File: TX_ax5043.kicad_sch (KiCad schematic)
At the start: 33 parts, among them P101 U_FL, U156 AX5043, U89 TPS22917DBV

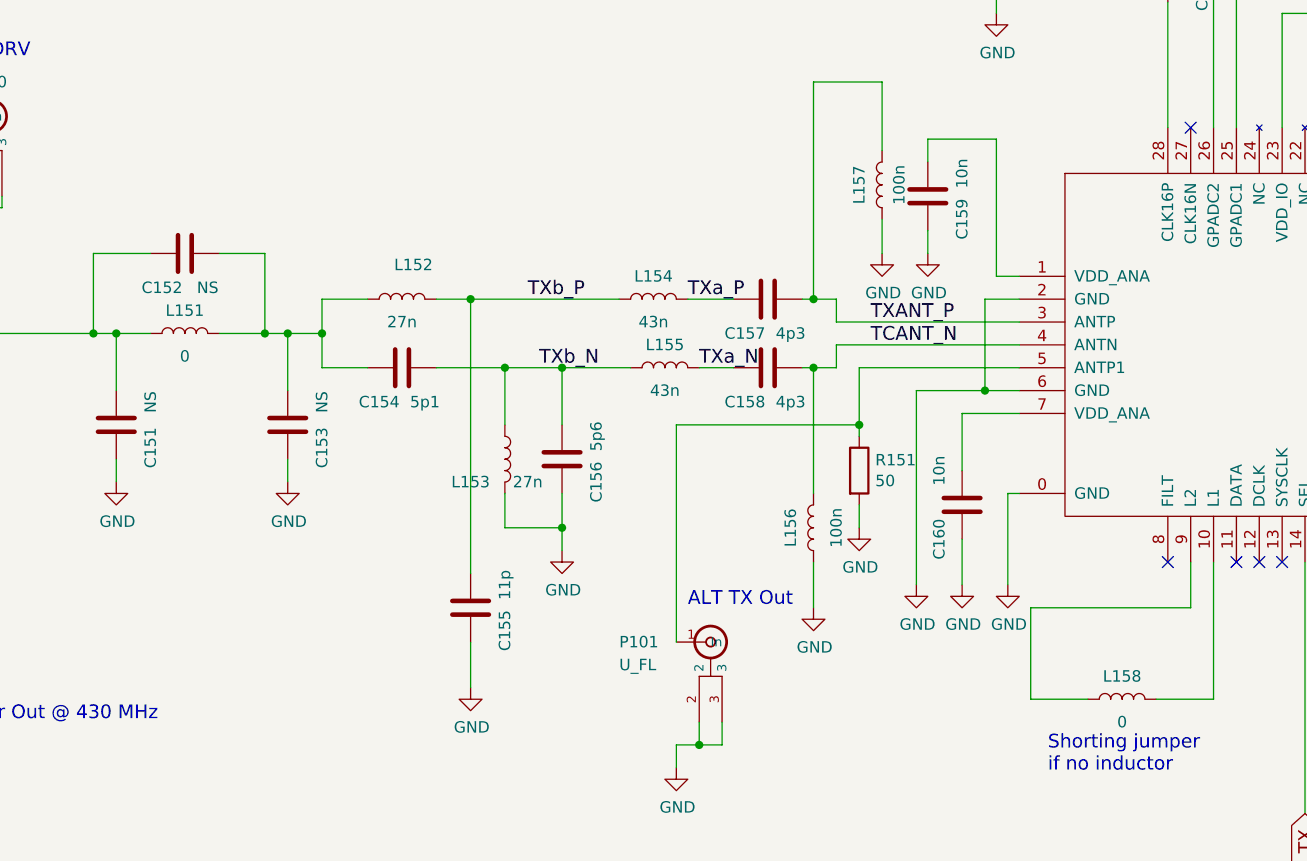
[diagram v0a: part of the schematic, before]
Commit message: Lots of cleanups to fix numerous issues
Signed-off-by: Corey Minyard <corey@minyard.net>
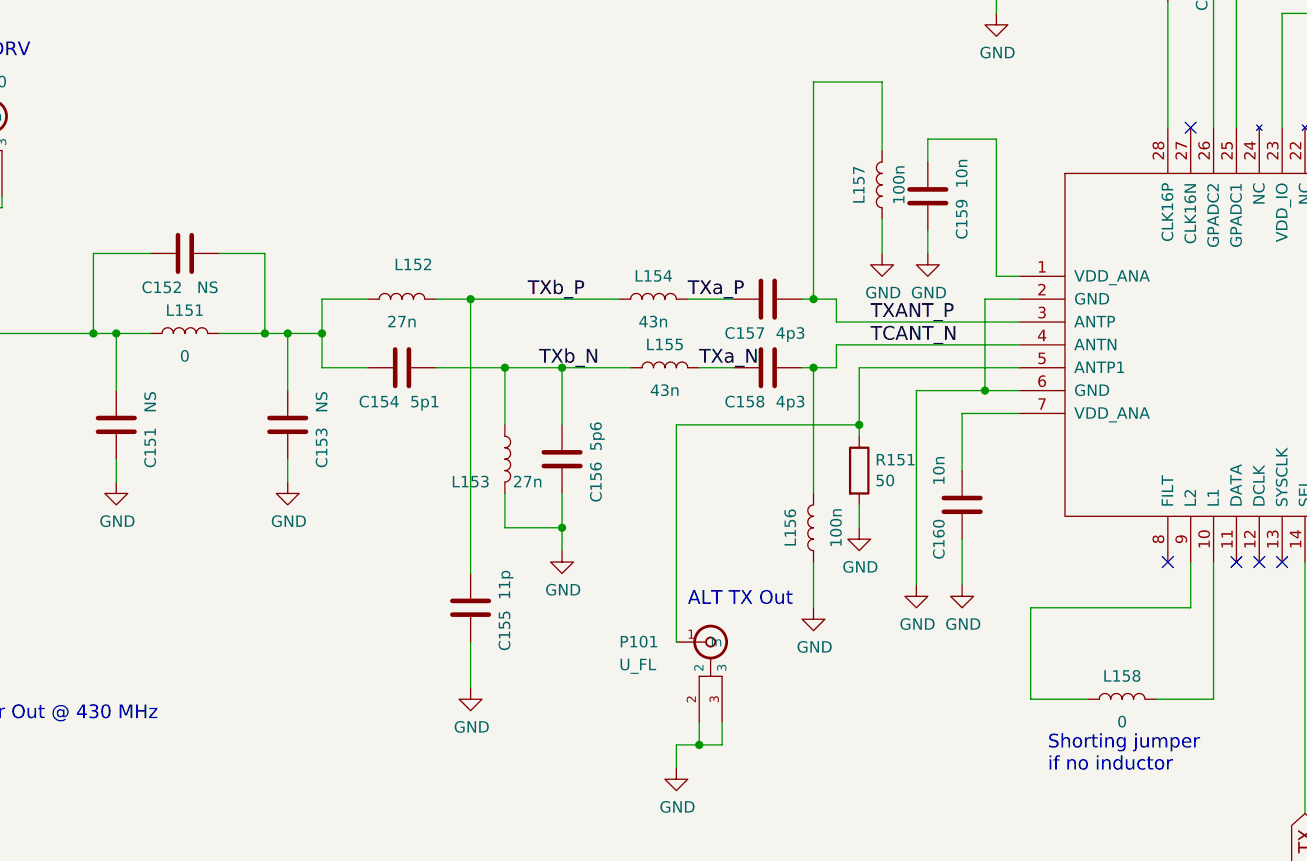
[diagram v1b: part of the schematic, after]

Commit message: More hacking on things
Signed-off-by: Corey Minyard <corey@minyard.net>
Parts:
- removed TP1, TP2: U_FL, PacSatDev_misc:U_FL SMD, symbol PACSAT_DEV_misc:U_FL
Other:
- note removed: "Test Structure"

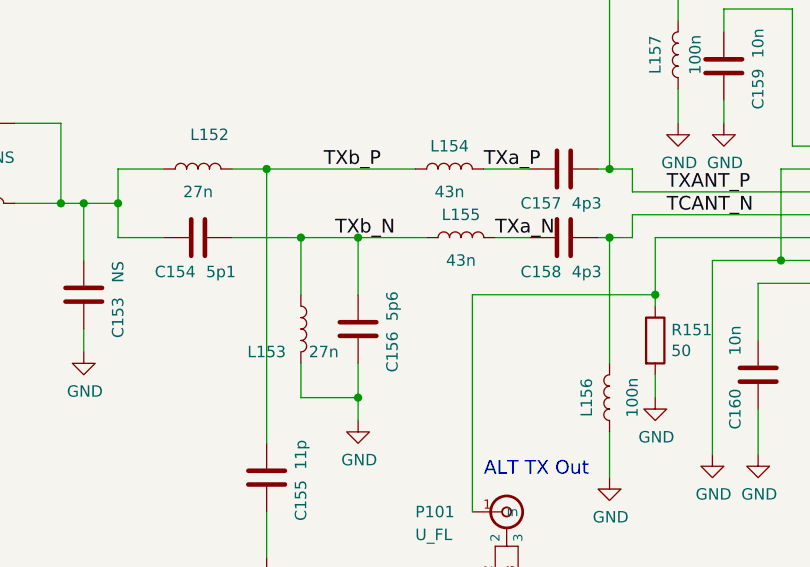
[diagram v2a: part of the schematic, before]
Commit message: Finish up most of the ax5043 routing
Signed-off-by: Corey Minyard <corey@minyard.net>
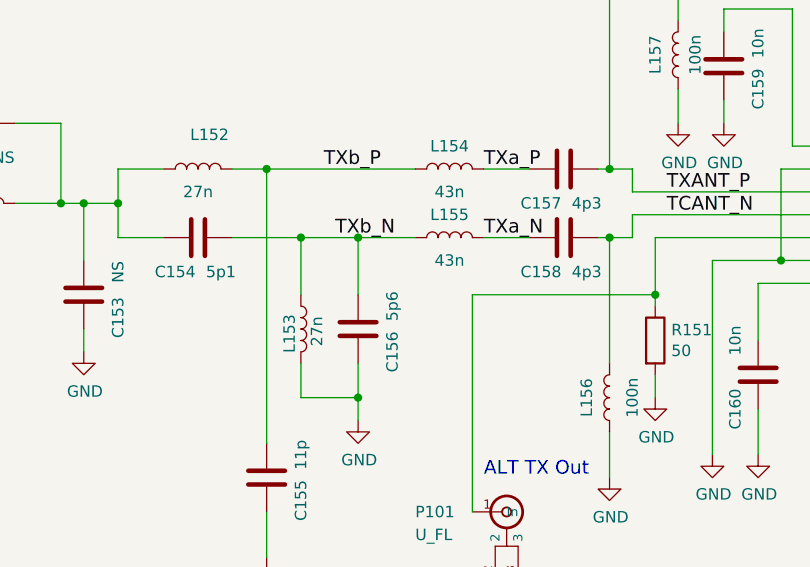
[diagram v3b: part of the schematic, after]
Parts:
- L151, L152, L153, L156, L157, L158: footprint PacSatDev_misc:L_Murata_LQH2MCNxxxx02_2.0x1.6mm -> Inductor_SMD:L_0603_1608Metric_Pad1.05x0.95mm_HandSolder
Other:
- moved on the sheet: L155
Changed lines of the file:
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@@
 	(wire
 		(pts
+			(xy 204.47 139.7) (xy 209.55 139.7)
+		)
+		(stroke
+			(width 0)
+			(type default)
+		)
+	)
+	(wire
+		(pts
 			(xy 163.83 139.7) (xy 168.91 139.7)
 		)
@@
 	(wire
 		(pts
-			(xy 190.5 139.7) (xy 198.12 139.7)
+			(xy 190.5 139.7) (xy 196.85 139.7)
 		)
 		(stroke
@@
 	(wire
 		(pts
-			(xy 205.74 139.7) (xy 209.55 139.7)
-		)
-		(stroke
-			(width 0)
-			(type default)
-		)
-	)
-	(wire
-		(pts
 			(xy 125.73 120.65) (xy 125.73 121.92)
 		)
@@
 	)
 	(label "TXa_N"
-		(at 205.74 139.7 0)
+		(at 204.47 139.7 0)
 		(effects
 			(font
@@
 		(dnp no)
 		(property "Reference" "L153"
-			(at 180.34 152.4 0)
+			(at 182.88 150.368 90)
 			(effects
 				(font
@@
 		)
 		(property "Value" "27n"
-			(at 186.69 152.4 0)
+			(at 185.928 150.114 90)
 			(effects
 				(font
@@
 			)
 		)
-		(property "Footprint" "PacSatDev_misc:L_Murata_LQH2MCNxxxx02_2.0x1.6mm"
+		(property "Footprint" "Inductor_SMD:L_0603_1608Metric_Pad1.05x0.95mm_HandSolder"
 			(at 184.15 149.86 0)
 			(effects
@@
 			)
 		)
-		(property "Footprint" "PacSatDev_misc:L_Murata_LQH2MCNxxxx02_2.0x1.6mm"
+		(property "Footprint" "Inductor_SMD:L_0603_1608Metric_Pad1.05x0.95mm_HandSolder"
 			(at 148.59 135.89 0)
 			(effects
@@
 	(symbol
 		(lib_id "Device:L")
-		(at 201.93 139.7 90)
+		(at 200.66 139.7 90)
 		(unit 1)
 		(exclude_from_sim no)
@@
 		(dnp no)
 		(property "Reference" "L155"
-			(at 201.93 137.16 90)
+			(at 200.66 137.16 90)
 			(effects
 				(font
@@
 		)
 		(property "Value" "43n"
-			(at 201.93 142.24 90)
+			(at 200.66 142.24 90)
 			(effects
 				(font
@@
 		)
 		(property "Footprint" "Inductor_SMD:L_0603_1608Metric_Pad1.05x0.95mm_HandSolder"
-			(at 201.93 139.7 0)
+			(at 200.66 139.7 0)
 			(effects
 				(font
@@
 		)
 		(property "Datasheet" "~"
-			(at 201.93 139.7 0)
+			(at 200.66 139.7 0)
 			(effects
 				(font
@@
 		)
 		(property "Description" ""
-			(at 201.93 139.7 0)
+			(at 200.66 139.7 0)
 			(effects
 				(font
@@
 			)
 		)
-		(property "Footprint" "PacSatDev_misc:L_Murata_LQH2MCNxxxx02_2.0x1.6mm"
+		(property "Footprint" "Inductor_SMD:L_0603_1608Metric_Pad1.05x0.95mm_HandSolder"
 			(at 226.06 119.38 0)
 			(effects
@@
 			)
 		)
-		(property "Footprint" "PacSatDev_misc:L_Murata_LQH2MCNxxxx02_2.0x1.6mm"
+		(property "Footprint" "Inductor_SMD:L_0603_1608Metric_Pad1.05x0.95mm_HandSolder"
 			(at 252.73 176.53 0)
 			(effects
@@
 			)
 		)
-		(property "Description" ""
+		(property "Description" "1V to 5.5V, 2A, 80mΩ Ultra-Low Leakage Load Switch, SOT23-6"
 			(at 346.71 80.01 0)
 			(effects
@@
 					(size 1.27 1.27)
 				)
+				(hide yes)
 			)
 		)
@@
 			)
 		)
-		(property "Footprint" "PacSatDev_misc:L_Murata_LQH2MCNxxxx02_2.0x1.6mm"
+		(property "Footprint" "Inductor_SMD:L_0603_1608Metric_Pad1.05x0.95mm_HandSolder"
 			(at 218.44 157.48 0)
 			(effects
@@
 			)
 		)
-		(property "Footprint" "PacSatDev_misc:L_Murata_LQH2MCNxxxx02_2.0x1.6mm"
+		(property "Footprint" "Inductor_SMD:L_0603_1608Metric_Pad1.05x0.95mm_HandSolder"
 			(at 172.72 132.08 0)
 			(effects

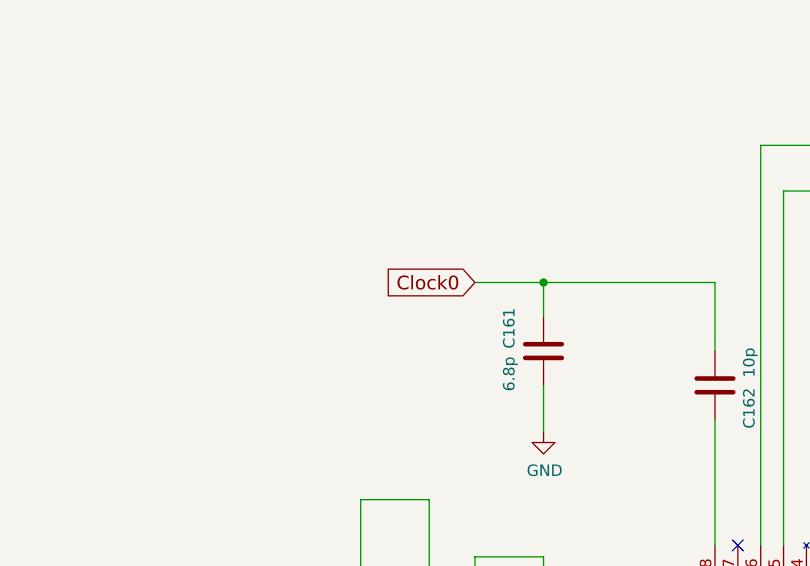
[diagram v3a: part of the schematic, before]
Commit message: Wire in clocks, more cleanups, wire in MRAM
Signed-off-by: Corey Minyard <corey@minyard.net>
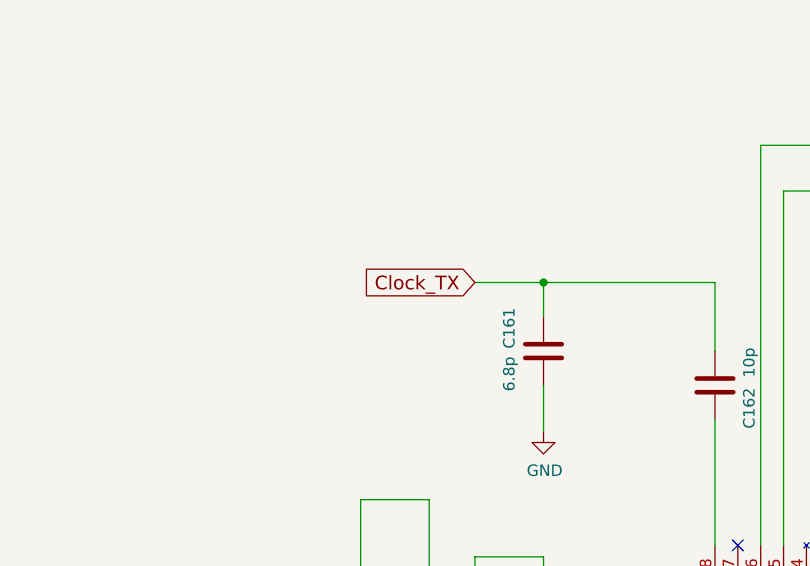
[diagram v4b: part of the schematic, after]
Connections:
- net Clock0 renamed Clock_TX
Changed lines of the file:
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@@
 		)
 	)
-	(global_label "Clock0"
+	(global_label "Clock_TX"
 		(shape input)
 		(at 231.14 83.82 180)
@@
 		)
 		(property "Intersheetrefs" "${INTERSHEET_REFS}"
-			(at 220.746 83.82 0)
+			(at 218.3284 83.82 0)
 			(effects
 				(font

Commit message: Finish up and clean up a lot of things
Signed-off-by: Corey Minyard <corey@minyard.net>
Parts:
- added R102: 1K, Resistor_SMD:R_0603_1608Metric_Pad0.98x0.95mm_HandSolder, symbol Device:R
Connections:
- net AX5043_CLK: now also R102.2; no longer U156.15 (CLK)
- new net: R102.1, U156.15 (CLK)
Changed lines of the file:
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@@
 	(wire
 		(pts
+			(xy 304.8 144.78) (xy 313.69 144.78)
+		)
+		(stroke
+			(width 0)
+			(type default)
+		)
+	)
+	(wire
+		(pts
 			(xy 152.4 135.89) (xy 157.48 135.89)
 		)
@@
 	(wire
 		(pts
-			(xy 289.56 144.78) (xy 293.37 144.78)
+			(xy 289.56 144.78) (xy 297.18 144.78)
 		)
 		(stroke
@@
 	(global_label "AX5043_CLK"
 		(shape input)
-		(at 293.37 144.78 0)
+		(at 313.69 144.78 0)
 		(fields_autoplaced yes)
 		(effects
@@
 		)
 		(property "Intersheetrefs" "${INTERSHEET_REFS}"
-			(at 310.0775 144.78 0)
+			(at 330.3975 144.78 0)
 			(effects
 				(font
@@
 					(unit 1)
 				)
+			)
+		)
+	)
+	(symbol
+		(lib_id "Device:R")
+		(at 300.99 144.78 90)
+		(unit 1)
+		(exclude_from_sim no)
+		(in_bom yes)
+		(on_board yes)
+		(dnp no)
+		(property "Reference" "R102"
+			(at 301.244 147.066 90)
+			(effects
+				(font
+					(size 1.27 1.27)
+				)
+			)
+		)
+		(property "Value" "1K"
+			(at 301.244 149.606 90)
+			(effects
+				(font
+					(size 1.27 1.27)
+				)
+			)
+		)
+		(property "Footprint" "Resistor_SMD:R_0603_1608Metric_Pad0.98x0.95mm_HandSolder"
+			(at 300.99 146.558 90)
+			(effects
+				(font
+					(size 1.27 1.27)
+				)
+				(hide yes)
+			)
+		)
+		(property "Datasheet" "~"
+			(at 300.99 144.78 0)
+			(effects
+				(font
+					(size 1.27 1.27)
+				)
+				(hide yes)
+			)
+		)
+		(property "Description" "Resistor"
+			(at 300.99 144.78 0)
+			(effects
+				(font
+					(size 1.27 1.27)
+				)
+				(hide yes)
+			)
+		)
+		(pin "1"
+		)
+		(pin "2"
+		)
+		(instances
+			(project "PacSat_AFSK"
+				(path "/cc9f42d2-6985-41ac-acab-5ab7b01c5b38/00000000-0000-0000-0000-00005a014be3"
+					(reference "R102")
+					(unit 1)
+				)

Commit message: Lots of notes and things about various items
Signed-off-by: Corey Minyard <corey@minyard.net>
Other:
- note added: "16 dBm Max Power Out @ 430 MHz If the PA works as expected, The maximum output here should be limited in the AX5043 to 13dBm to avoid overdriving the PA."
- note removed: "16 dB Max Power Out @ 430 MHz"
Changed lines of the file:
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@@
 		)
 	)
-	(text "16 dB Max Power Out @ 430 MHz"
+	(text "16 dBm Max Power Out @ 430 MHz\nIf the PA works as expected,\nThe maximum output here should\nbe limited in the AX5043 to 13dBm\nto avoid overdriving the PA."
 		(exclude_from_sim no)
 		(at 110.49 179.07 0)
